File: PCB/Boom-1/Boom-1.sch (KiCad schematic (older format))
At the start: 720 parts, among them U1 CEM3340, U10 AS3320, U11 AS3310, U12 AS3310, U13 AS3310, U14 AS3310, U15 V2164D, U16 AS3310, U17 AS3310, U18 V2164D, U19 TL074, U2 CEM3340, U20 TL074, U21 TL074, U22 TL074, U23 TL074, U24 TL074, U25 TL074, U26 TL074, U27 TL072, U28 TL074, U29 TL072, U3 4013, U30 TL074, U31 TL072, U32 TL074, U33 TL074, U34 TL074, U35 TL072, U36 TL074, U37 TL074, U38 TL072, U4 NOISE, U5 V2164D, U6 V2164D, U7 V2164D, U8 AS3320, U9 AS3320

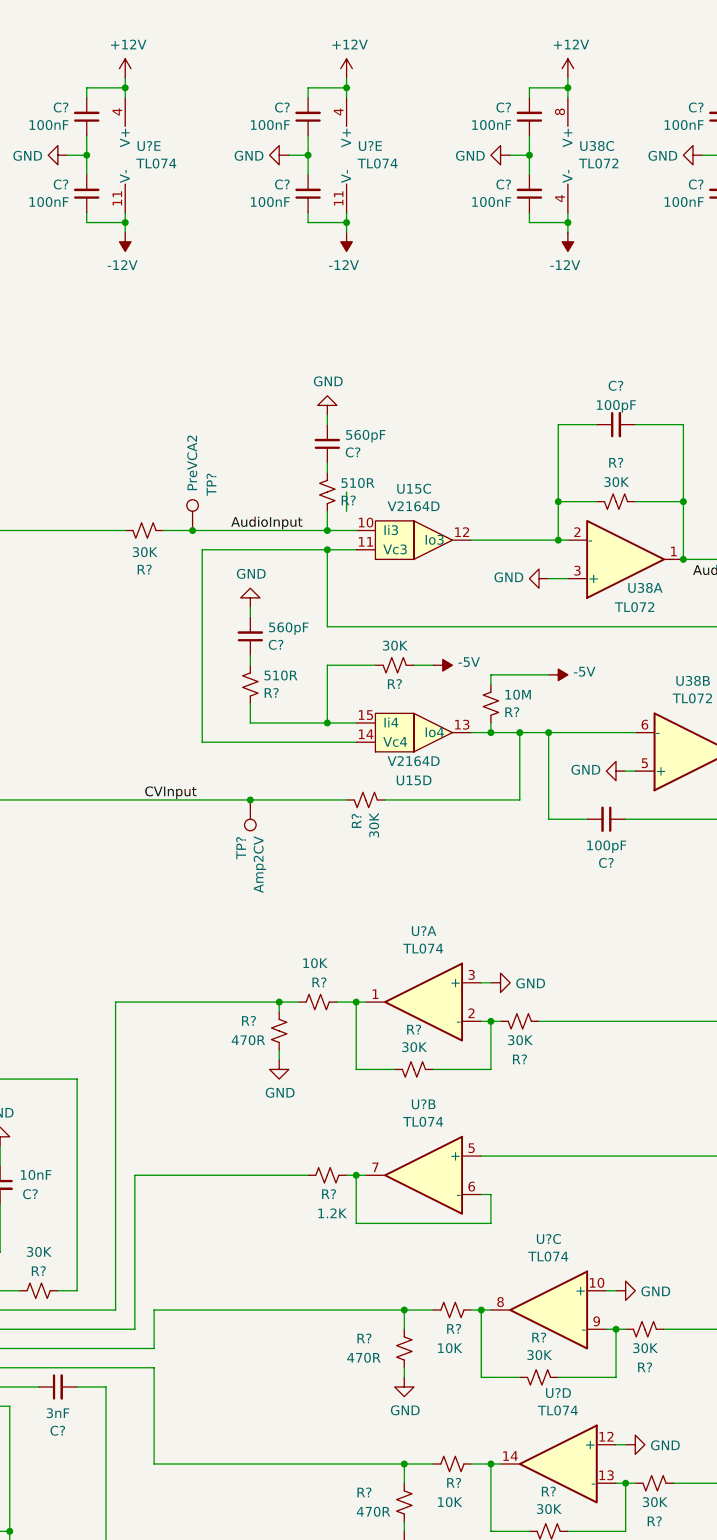
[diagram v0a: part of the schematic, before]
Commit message: U39 is TL074 normalizing ADSR in sub amp env
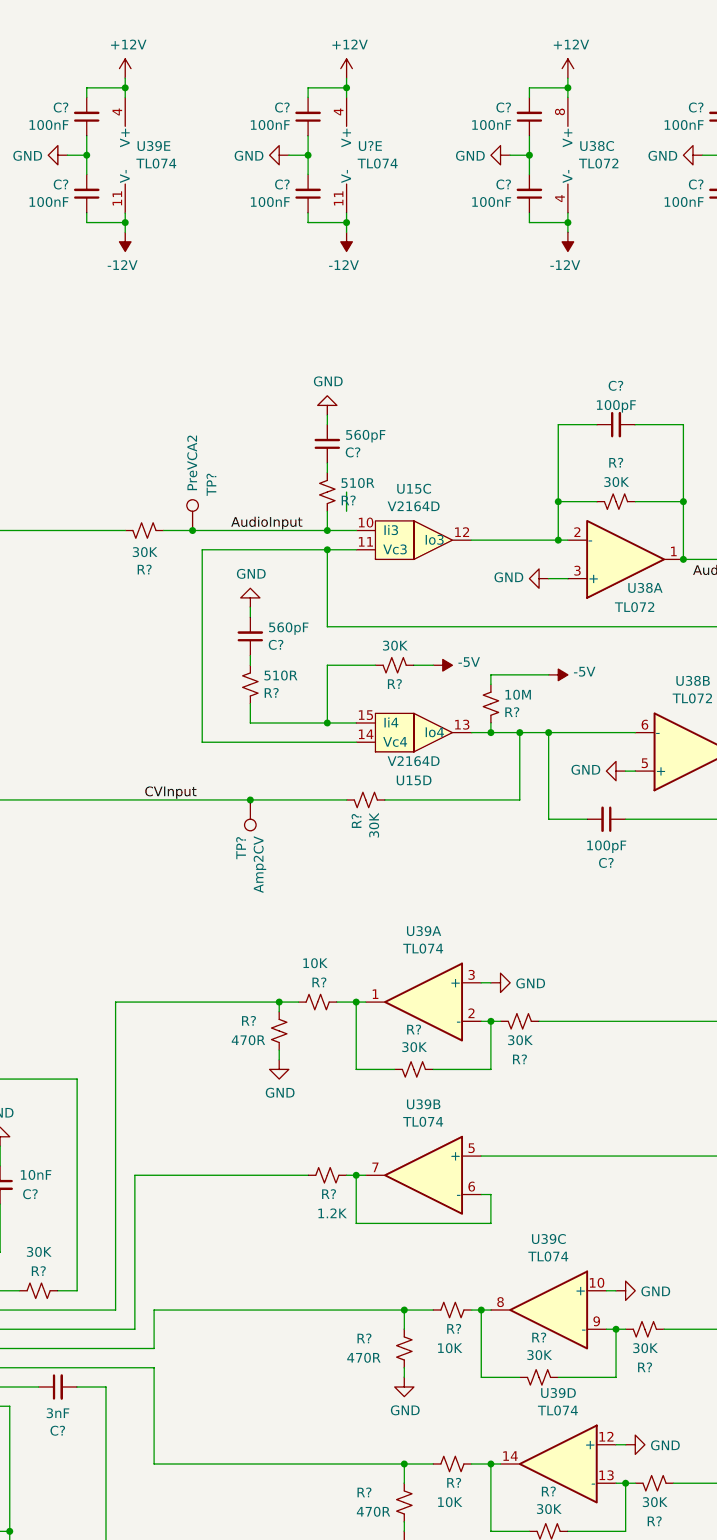
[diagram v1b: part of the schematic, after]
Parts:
- gave numbers to parts that had none: 1
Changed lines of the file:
@@
 $EndComp
 $Comp
-L Amplifier_Operational:TL074 U?
+L Amplifier_Operational:TL074 U39
 U 1 1 6983136F
 P 34500 39800
-F 0 "U?" H 34500 40167 50  0000 C CNN
+F 0 "U39" H 34500 40167 50  0000 C CNN
 F 1 "TL074" H 34500 40076 50  0000 C CNN
 F 2 "" H 34450 39900 50  0001 C CNN
@@
 $EndComp
 $Comp
-L Amplifier_Operational:TL074 U?
+L Amplifier_Operational:TL074 U39
 U 2 1 69838EBC
 P 34500 40700
-F 0 "U?" H 34500 41067 50  0000 C CNN
+F 0 "U39" H 34500 41067 50  0000 C CNN
 F 1 "TL074" H 34500 40976 50  0000 C CNN
 F 2 "" H 34450 40800 50  0001 C CNN
@@
 $EndComp
 $Comp
-L Amplifier_Operational:TL074 U?
+L Amplifier_Operational:TL074 U39
 U 3 1 6984168A
 P 35150 41400
-F 0 "U?" H 35150 41767 50  0000 C CNN
+F 0 "U39" H 35150 41767 50  0000 C CNN
 F 1 "TL074" H 35150 41676 50  0000 C CNN
 F 2 "" H 35100 41500 50  0001 C CNN
@@
 $EndComp
 $Comp
-L Amplifier_Operational:TL074 U?
+L Amplifier_Operational:TL074 U39
 U 4 1 698496C4
 P 35200 42200
-F 0 "U?" H 35200 42567 50  0000 C CNN
+F 0 "U39" H 35200 42567 50  0000 C CNN
 F 1 "TL074" H 35200 42476 50  0000 C CNN
 F 2 "" H 35150 42300 50  0001 C CNN
@@
 	35250 35050 35250 35100
 $Comp
-L Amplifier_Operational:TL074 U?
+L Amplifier_Operational:TL074 U39
 U 5 1 7A9C989D
 P 33050 35400
-F 0 "U?" H 33008 35446 50  0000 L CNN
+F 0 "U39" H 33008 35446 50  0000 L CNN
 F 1 "TL074" H 33008 35355 50  0000 L CNN
 F 2 "" H 33000 35500 50  0001 C CNN

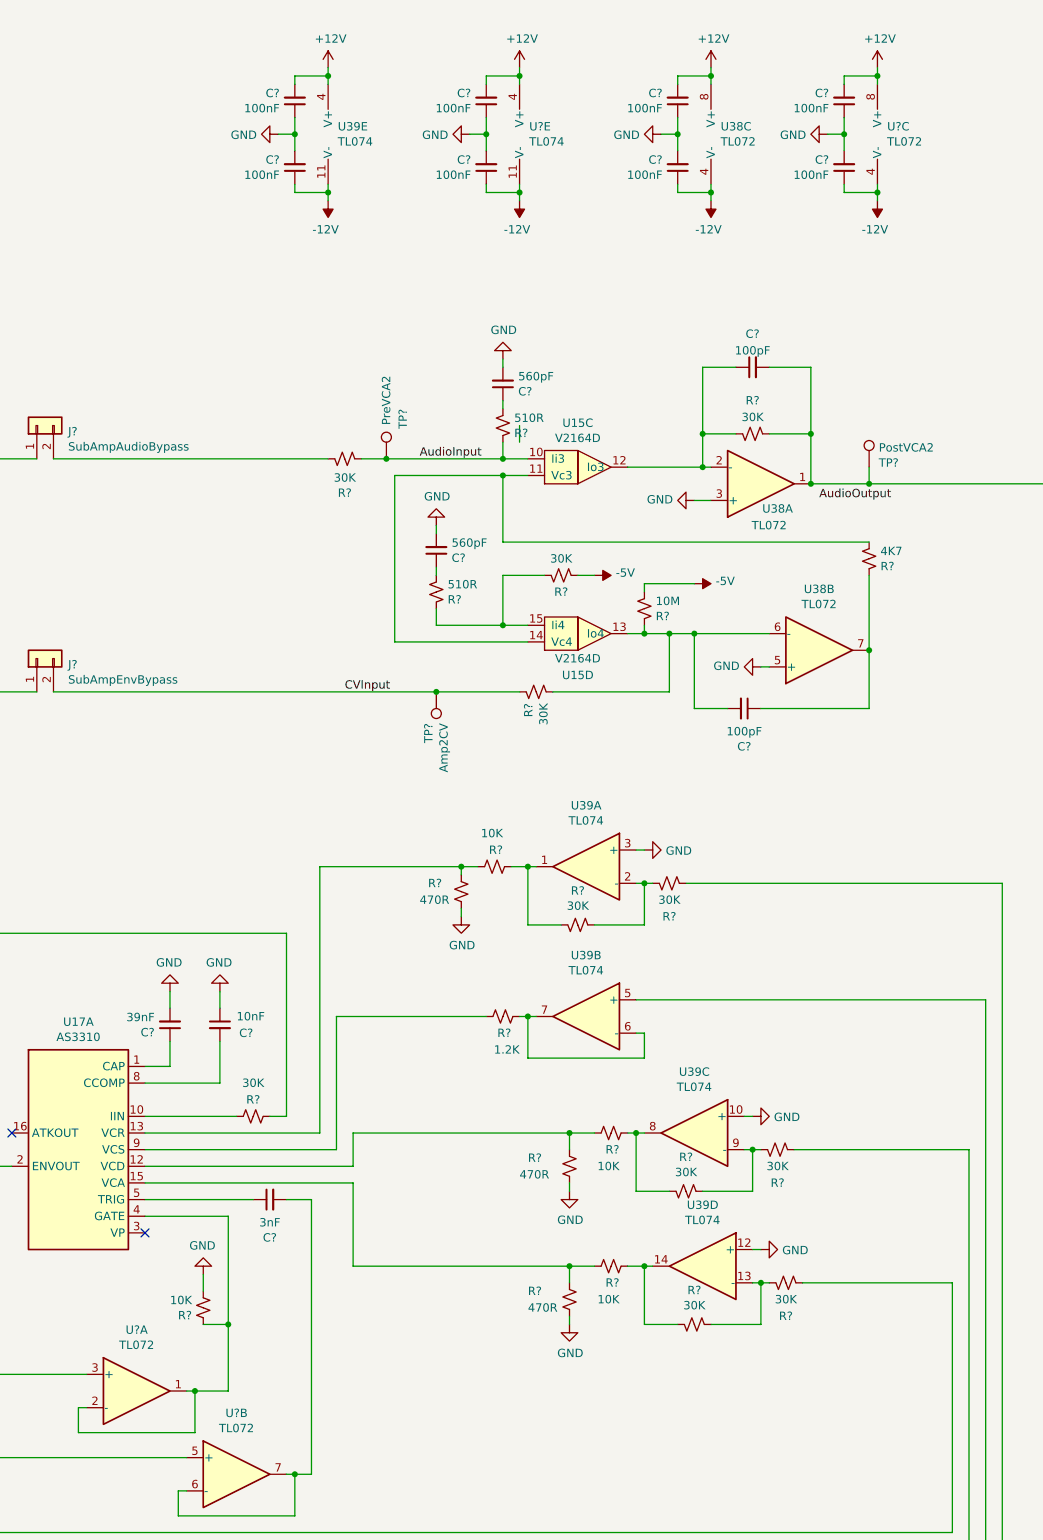
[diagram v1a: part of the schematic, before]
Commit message: U40 is trig and gate buffer for osc amp env
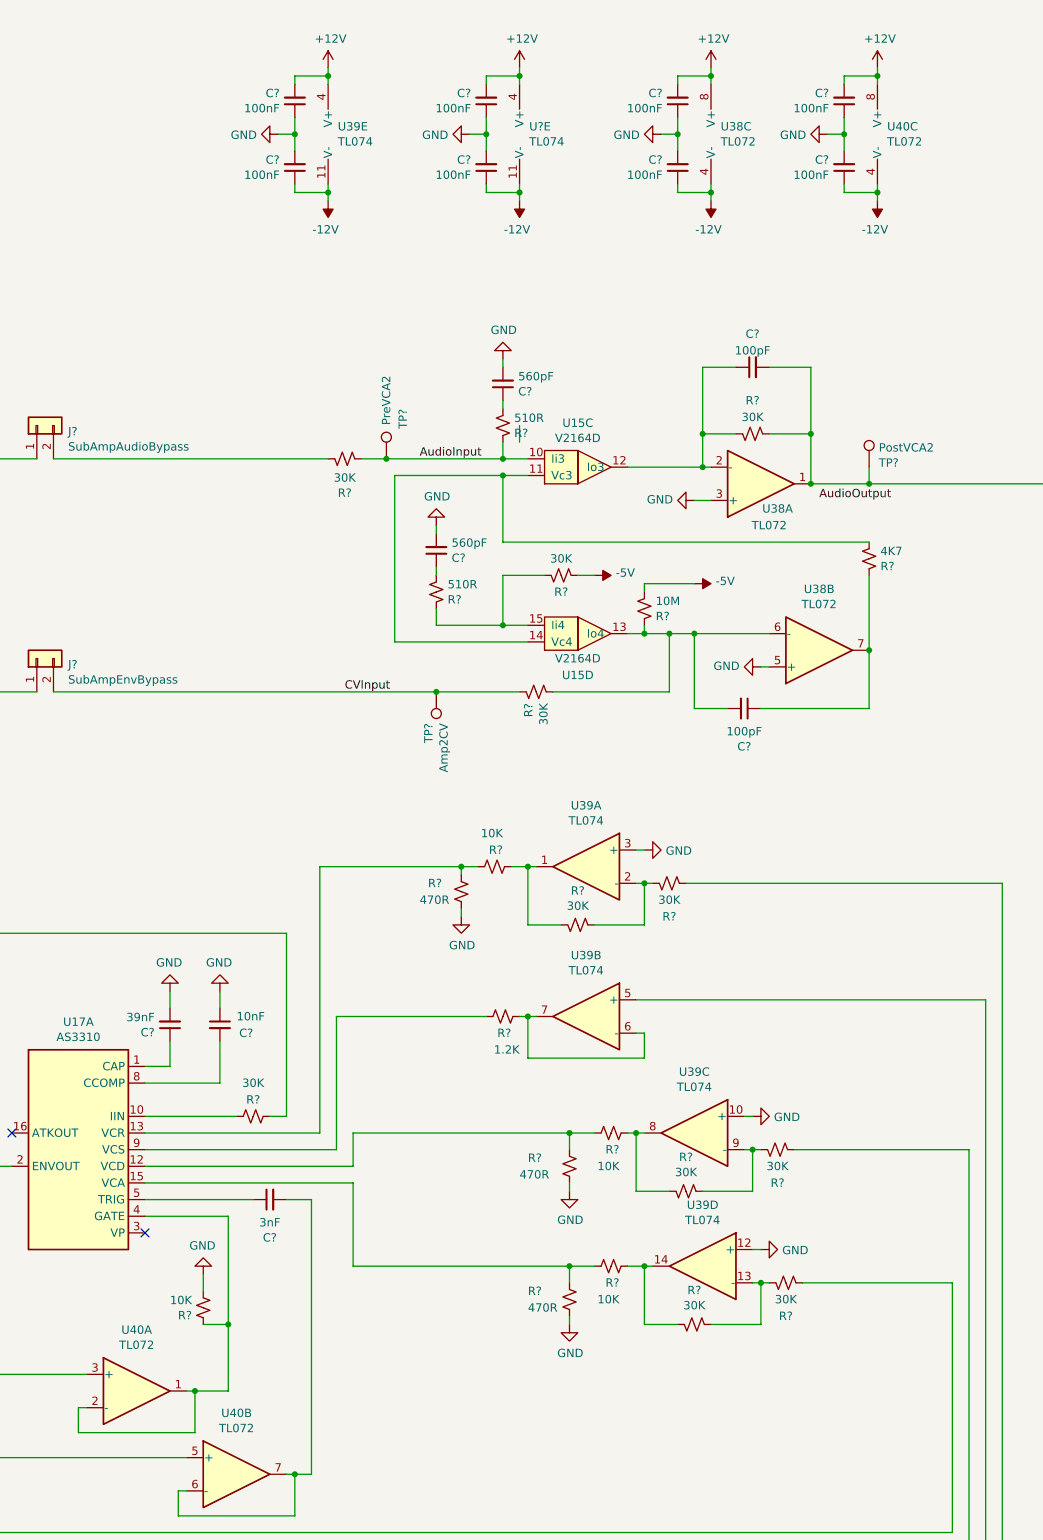
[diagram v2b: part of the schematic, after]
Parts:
- gave numbers to parts that had none: 1
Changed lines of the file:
@@
 $EndComp
 $Comp
-L Amplifier_Operational:TL072 U?
+L Amplifier_Operational:TL072 U40
 U 1 1 698528F2
 P 31800 42950
-F 0 "U?" H 31800 43317 50  0000 C CNN
+F 0 "U40" H 31800 43317 50  0000 C CNN
 F 1 "TL072" H 31800 43226 50  0000 C CNN
 F 2 "" H 31800 42950 50  0001 C CNN
@@
 $EndComp
 $Comp
-L Amplifier_Operational:TL072 U?
+L Amplifier_Operational:TL072 U40
 U 2 1 6985BC72
 P 32400 43450
-F 0 "U?" H 32400 43817 50  0000 C CNN
+F 0 "U40" H 32400 43817 50  0000 C CNN
 F 1 "TL072" H 32400 43726 50  0000 C CNN
 F 2 "" H 32400 43450 50  0001 C CNN
@@
 	36200 38500 36200 38850
 $Comp
-L Amplifier_Operational:TL072 U?
+L Amplifier_Operational:TL072 U40
 U 3 1 69017537
 P 36350 35400
-F 0 "U?" H 36308 35446 50  0000 L CNN
+F 0 "U40" H 36308 35446 50  0000 L CNN
 F 1 "TL072" H 36308 35355 50  0000 L CNN
 F 2 "" H 36350 35400 50  0001 C CNN
